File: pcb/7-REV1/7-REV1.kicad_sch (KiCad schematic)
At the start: 11 parts

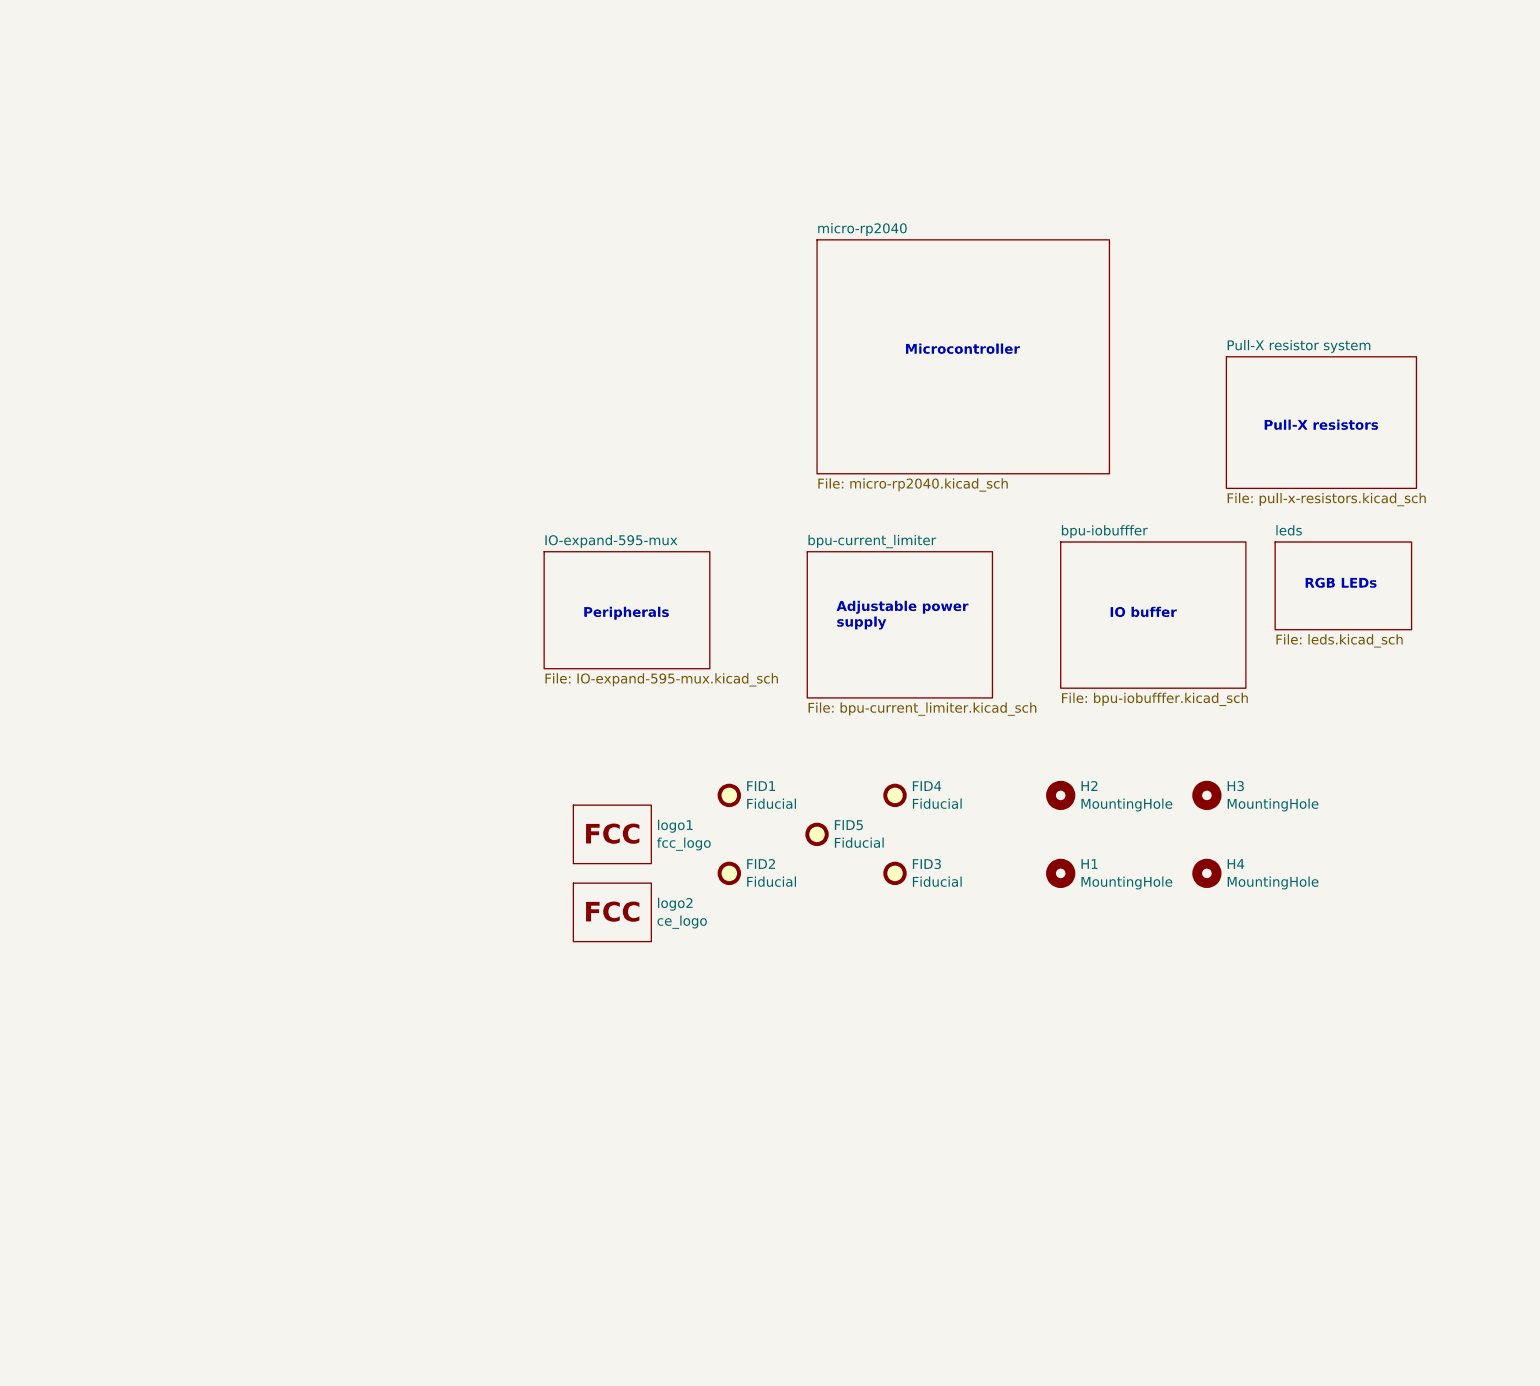
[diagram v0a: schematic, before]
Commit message: Add VOUT protection from electronic_eel: https://forum.buspirate.com/t/port-protection-for-rev7/712/37 . Minor cleanup of top page.
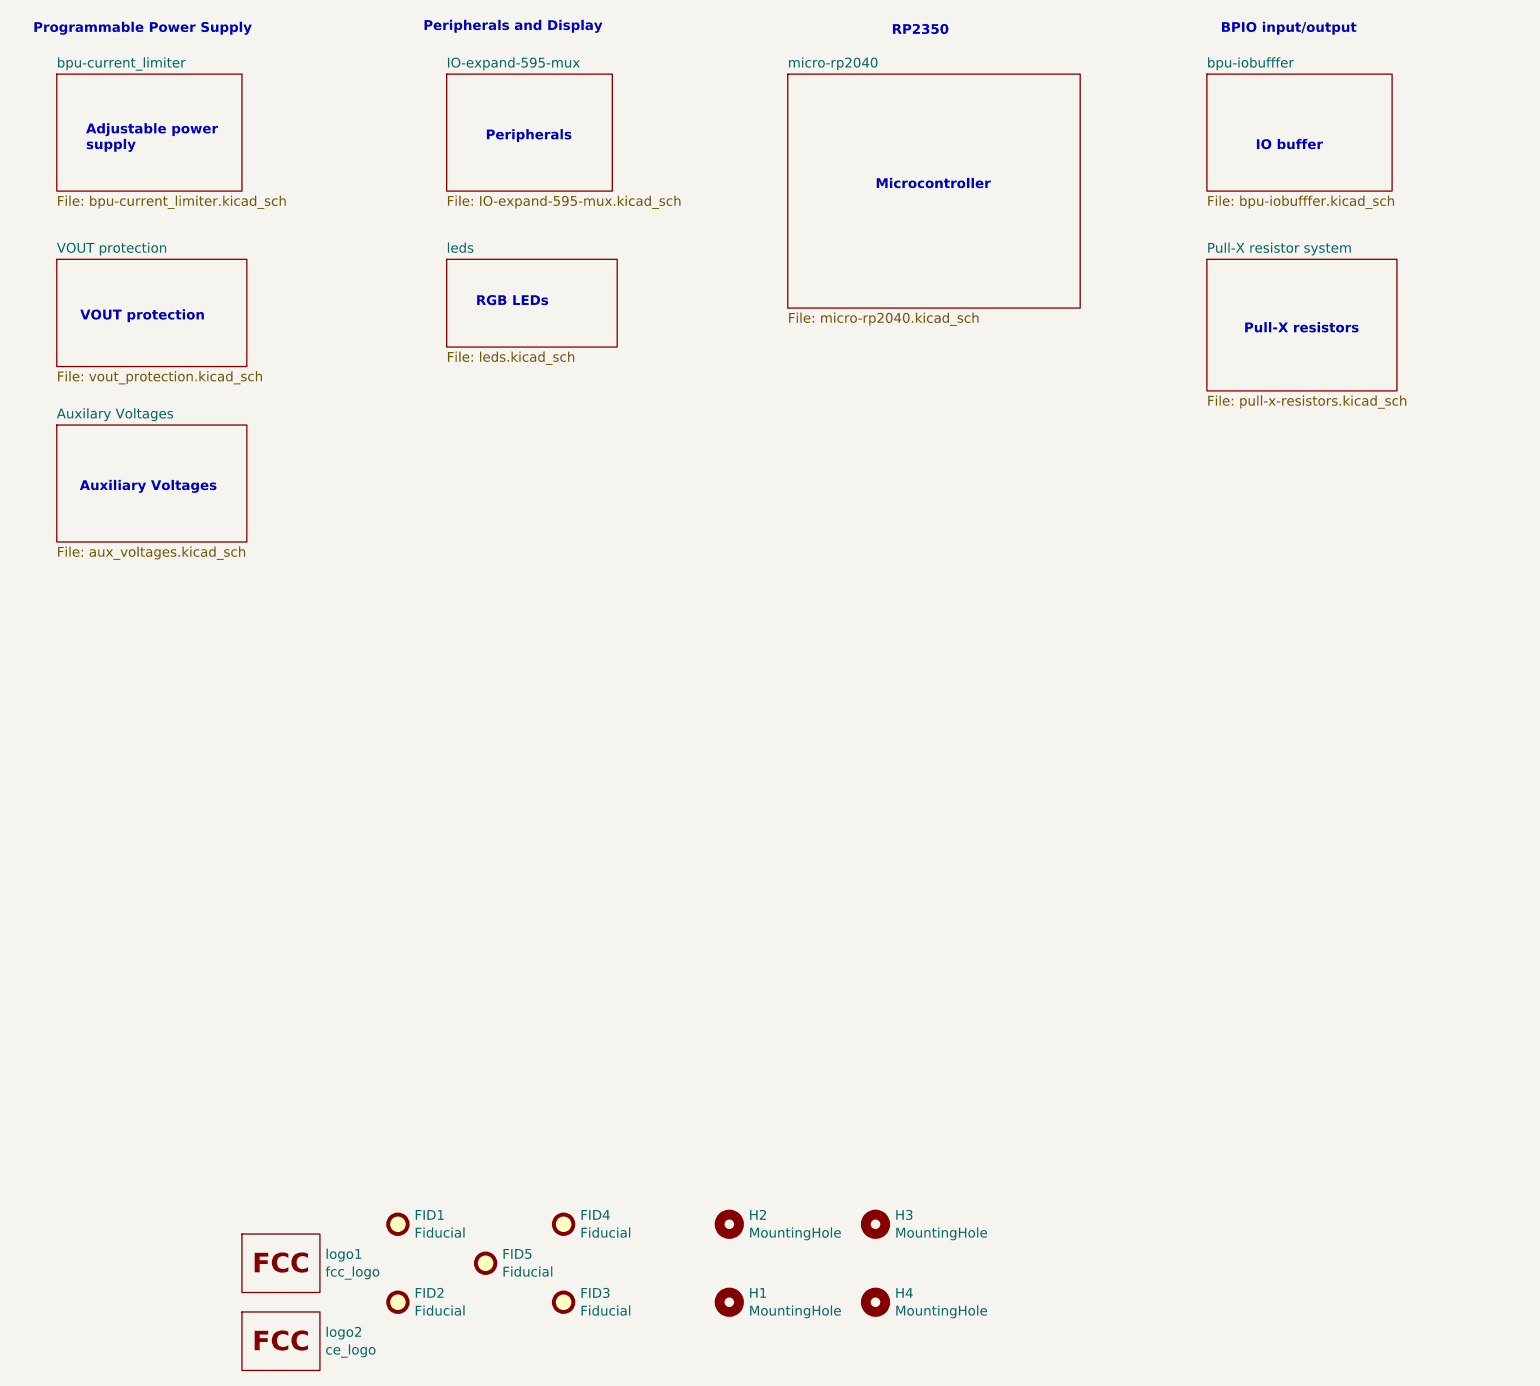
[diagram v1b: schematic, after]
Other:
- added sheet Auxilary Voltages (aux_voltages.kicad_sch)
- added sheet VOUT protection (vout_protection.kicad_sch)
- note added: "Auxiliary Voltages"
- note added: "BPIO input/output"
- note added: "Peripherals and Display"
- note added: "Programmable Power Supply"
- note added: "RP2350"
- note added: "VOUT protection"
- moved on the sheet: FID1, FID2, FID3, FID4, FID5, H1, H2, H3, H4, logo1, logo2

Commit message: reorg, but forgot to check changes first :(
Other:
- removed sheet Auxilary Voltages
- removed sheet VOUT protection
- note removed: "Auxiliary Voltages"
- note removed: "VOUT protection"
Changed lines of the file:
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@@
 	(generator_version "8.0")
 	(paper "A4")
-	(text "VOUT protection"
-		(exclude_from_sim no)
-		(at 32.766 54.483 0)
-		(effects
-			(font
-				(size 1.27 1.27)
-				(thickness 0.254)
-				(bold yes)
-			)
-		)
-	)
 	(text "Microcontroller"
 		(exclude_from_sim no)
@@
 		(exclude_from_sim no)
 		(at 134.112 17.272 0)
-		(effects
-			(font
-				(size 1.27 1.27)
-				(thickness 0.254)
-				(bold yes)
-			)
-		)
-	)
-	(text "Auxiliary Voltages\n"
-		(exclude_from_sim no)
-		(at 33.528 76.708 0)
 		(effects
 			(font
@@
 				)
 			)
-		)
-	)
-	(sheet
-		(at 21.59 46.99)
-		(size 24.765 13.97)
-		(fields_autoplaced yes)
-		(stroke
-			(width 0.1524)
-			(type solid)
-		)
-		(fill
-			(color 0 0 0 0.0000)
-		)
-		(property "Sheetname" "VOUT protection"
-			(at 21.59 46.2784 0)
-			(effects
-				(font
-					(size 1.27 1.27)
-				)
-				(justify left bottom)
-			)
-		)
-		(property "Sheetfile" "vout_protection.kicad_sch"
-			(at 21.59 61.5446 0)
-			(effects
-				(font
-					(size 1.27 1.27)
-				)
-				(justify left top)
-			)
-		)
-		(instances
-			(project "7-REV1"
-				(path "/1f56410a-eaac-4444-b0f7-cfd3531e22ac"
-					(page "9")
-				)
-			)
-		)
-	)
-	(sheet
-		(at 21.59 68.58)
-		(size 24.765 15.24)
-		(fields_autoplaced yes)
-		(stroke
-			(width 0.1524)
-			(type solid)
-		)
-		(fill
-			(color 0 0 0 0.0000)
-		)
-		(property "Sheetname" "Auxilary Voltages"
-			(at 21.59 67.8684 0)
-			(effects
-				(font
-					(size 1.27 1.27)
-				)
-				(justify left bottom)
-			)
-		)
-		(property "Sheetfile" "aux_voltages.kicad_sch"
-			(at 21.59 84.4046 0)
-			(effects
-				(font
-					(size 1.27 1.27)
-				)
-				(justify left top)
-			)
-		)
-		(instances
-			(project "7-REV1"
-				(path "/1f56410a-eaac-4444-b0f7-cfd3531e22ac"
-					(page "8")
-				)
-			)
